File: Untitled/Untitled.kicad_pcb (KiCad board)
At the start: 2 copper layers, 8 parts

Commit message: version1
I wanna figure out how to reduce the size somehow. but this version should work fine
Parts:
- added 12v_in1: 12v_in, TestPoint:TestPoint_Pad_D2.5mm, F.Cu at (197.5, 78.1)
- added GND_in1: GND_in, TestPoint:TestPoint_Pad_D2.5mm, F.Cu at (192.4, 78.1)
- added g_out1: g_out1, TestPoint:TestPoint_Plated_Hole_D2.0mm, F.Cu at (213.9, 99.5)
- added g_out2: g_out2, TestPoint:TestPoint_Plated_Hole_D2.0mm, F.Cu at (213.9, 95.5)
- added g_out3: g_out3, TestPoint:TestPoint_Plated_Hole_D2.0mm, F.Cu at (213.9, 91.5)
- added v_out1: vout_1, TestPoint:TestPoint_Plated_Hole_D2.0mm, F.Cu at (213.8, 86.2)
- added v_out2: vout_2, TestPoint:TestPoint_Plated_Hole_D2.0mm, F.Cu at (213.8, 82.2)
- added vout_3: vout_3, TestPoint:TestPoint_Plated_Hole_D2.0mm, F.Cu at (213.8, 78.2)
- moved C2 47.9 mm to (202.3, 90.1), turned to 90 degrees
- moved R2 47.3 mm to (207.6, 81.3), turned to -90 degrees
- moved C4 44.4 mm to (204.4, 78.2), turned to 180 degrees
- moved R1 44.2 mm to (204.4, 79.8)
- moved C1 42.9 mm to (196.7, 87.2), turned to 180 degrees
- moved C3 39.8 mm to (196.7, 85.7), turned to 180 degrees
- moved L1 33.7 mm to (202.6, 84.5), turned to -90 degrees
- moved VR1 30.4 mm to (197.7, 89.7)
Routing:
- net +5V: track 0.00 -> 34.1 mm
- net Net-(VR1-VFB): track 0.00 -> 24.4 mm
- net Net-(VR1-SW): track 0.00 -> 18.8 mm, vias 0 -> 2
- net +12V: track 0.00 -> 15.3 mm
- net GND: track 0.00 -> 6.90 mm, vias 0 -> 3
- net Net-(VR1-VBST): track 0.00 -> 4.28 mm
- added copper zone on B.Cu, net GND
- added copper zone on F.Cu, net GND
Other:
- board outline added: 26 x 26.7 mm

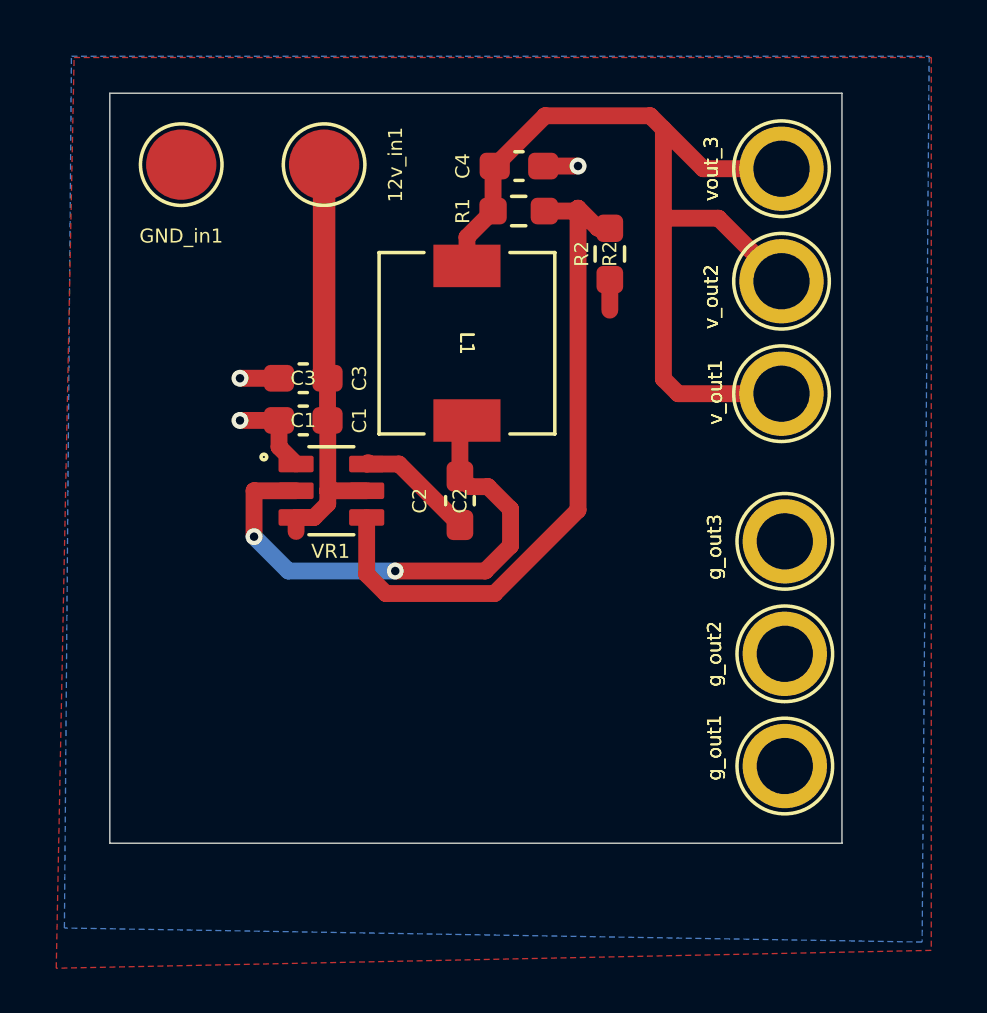
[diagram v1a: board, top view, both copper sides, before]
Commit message: updated c4 to 1206
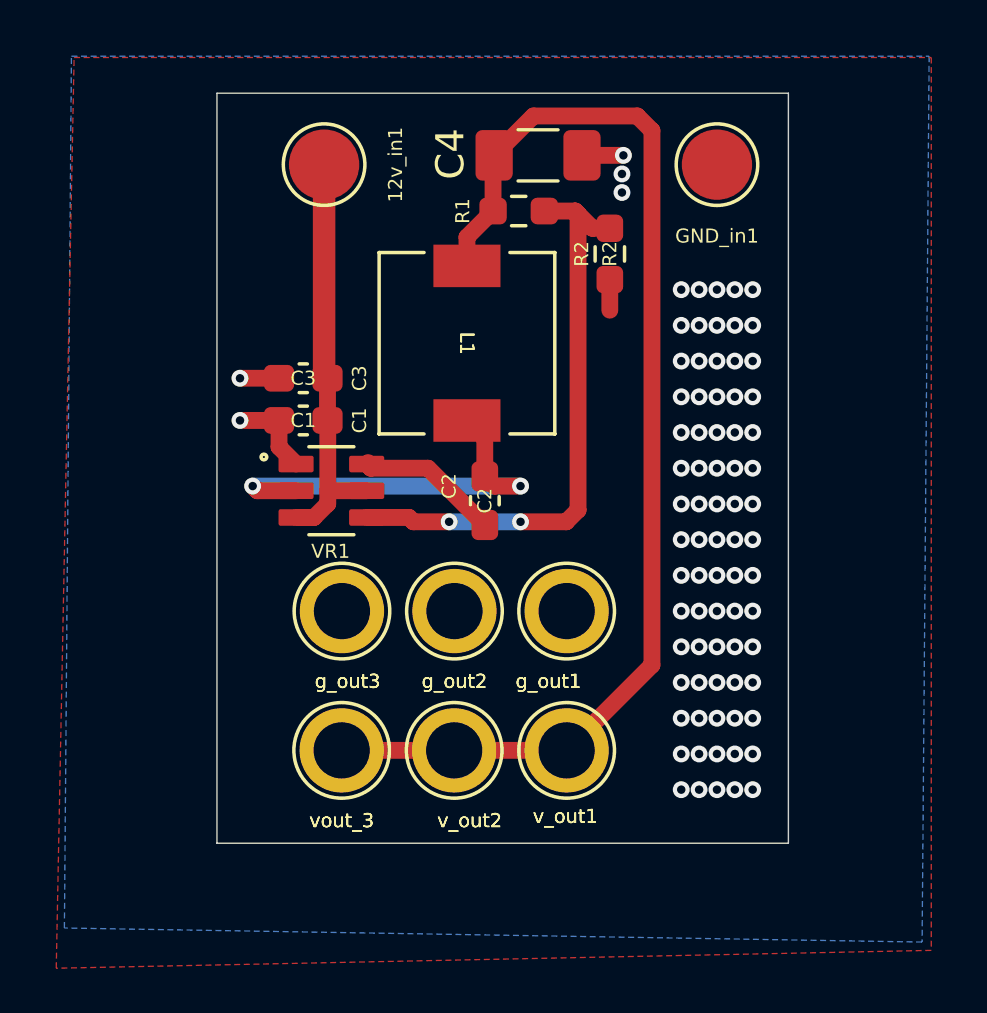
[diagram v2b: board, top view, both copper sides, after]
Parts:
- C4: footprint Capacitor_SMD:C_0603_1608Metric_Pad1.08x0.95mm_HandSolder -> Capacitor_SMD:C_1206_3216Metric_Pad1.33x1.80mm_HandSolder
- moved vout_3 25.9 mm to (198.1, 98.9), turned to 180 degrees
- moved v_out2 20.3 mm to (202.1, 98.9), turned to 180 degrees
- moved GND_in1 19.1 mm to (211.5, 78.1)
- moved g_out3 15.9 mm to (198.1, 94.0), turned to 0 degrees
- moved v_out1 14.8 mm to (206.1, 98.9), turned to 180 degrees
- moved g_out2 11.8 mm to (202.1, 94.0), turned to 180 degrees
- moved g_out1 9.52 mm to (206.1, 94.0), turned to 0 degrees
- moved C2 0.88 mm to (203.2, 90.1)
- moved C4 0.78 mm to (205.1, 77.8)
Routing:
- net +5V: track 34.1 -> 42.0 mm
- net Net-(VR1-SW): track 18.8 -> 15.2 mm
- net Net-(VR1-VFB): track 24.4 -> 21.0 mm, vias 0 -> 2
- net Net-(VR1-VBST): track 4.28 -> 5.17 mm
- net GND: track 6.90 -> 7.14 mm, vias 3 -> 80
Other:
- board size 26 x 26.7 mm -> 20.3 x 26.7 mm

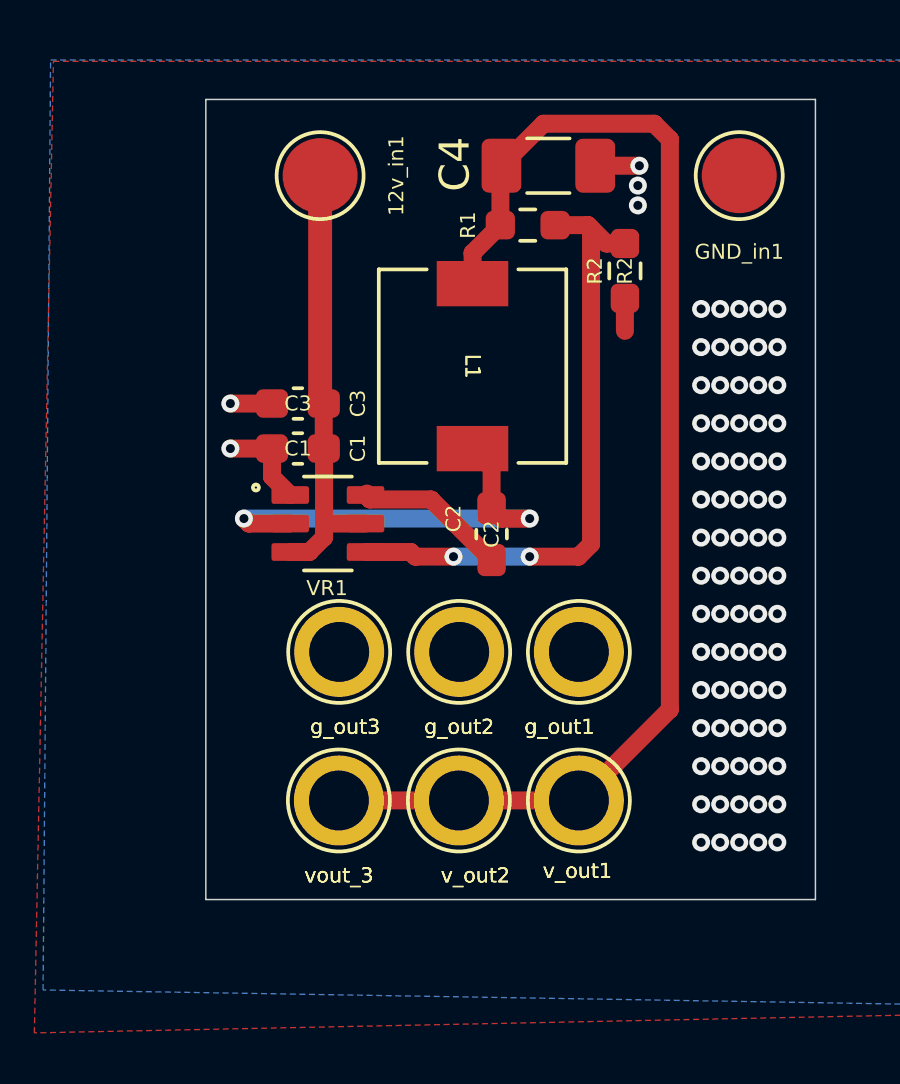
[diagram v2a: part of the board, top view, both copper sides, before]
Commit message: updated to 2.54tht pads
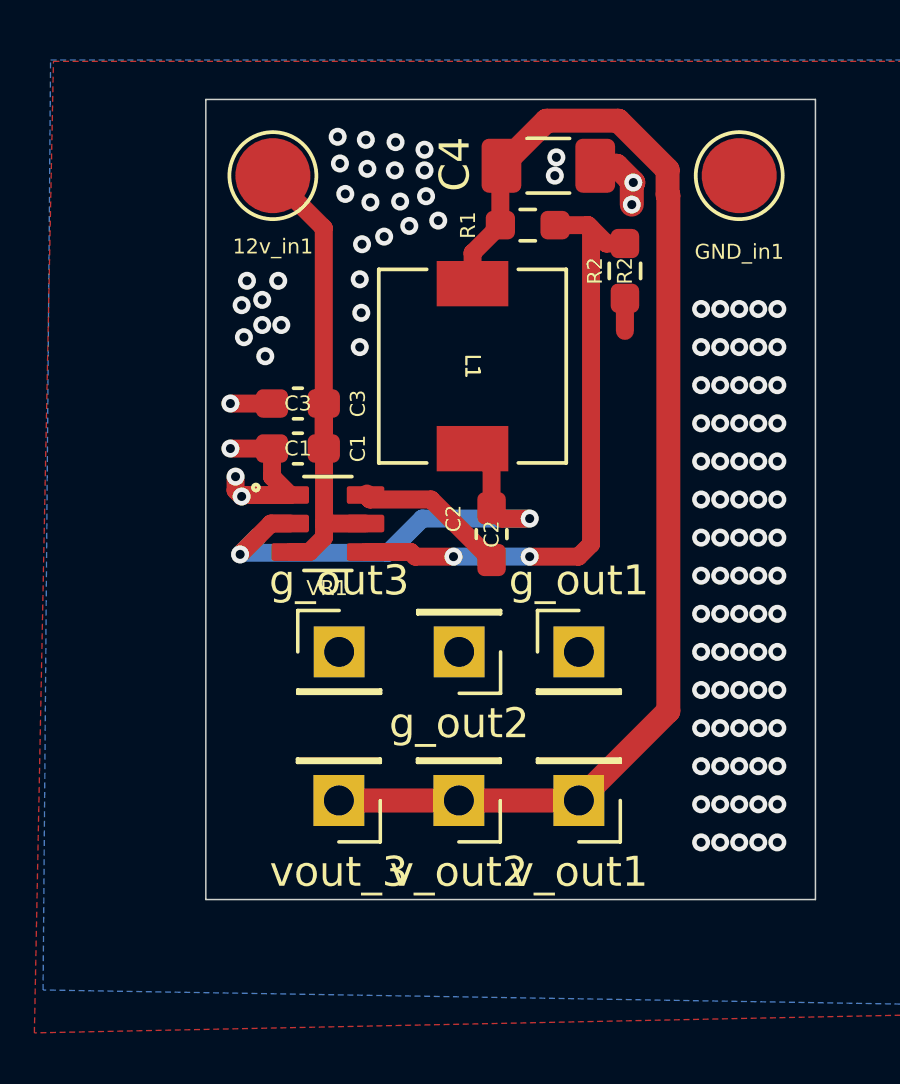
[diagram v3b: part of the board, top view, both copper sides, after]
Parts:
- g_out1, g_out2, g_out3, v_out1, v_out2, vout_3: footprint TestPoint:TestPoint_Plated_Hole_D2.0mm -> Connector_PinHeader_2.54mm:PinHeader_1x01_P2.54mm_Vertical
- moved 12v_in1 1.57 mm to (195.9, 78.1)
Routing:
- net GND: track 7.14 -> 10.3 mm, vias 80 -> 110
- net +12V: track 14.8 -> 17.6 mm
- net Net-(VR1-SW): track 15.2 -> 17.1 mm
- net +5V: track 42.0 -> 41.4 mm
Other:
- board text added: "Designed by Caleb Murray IEEE 2026"

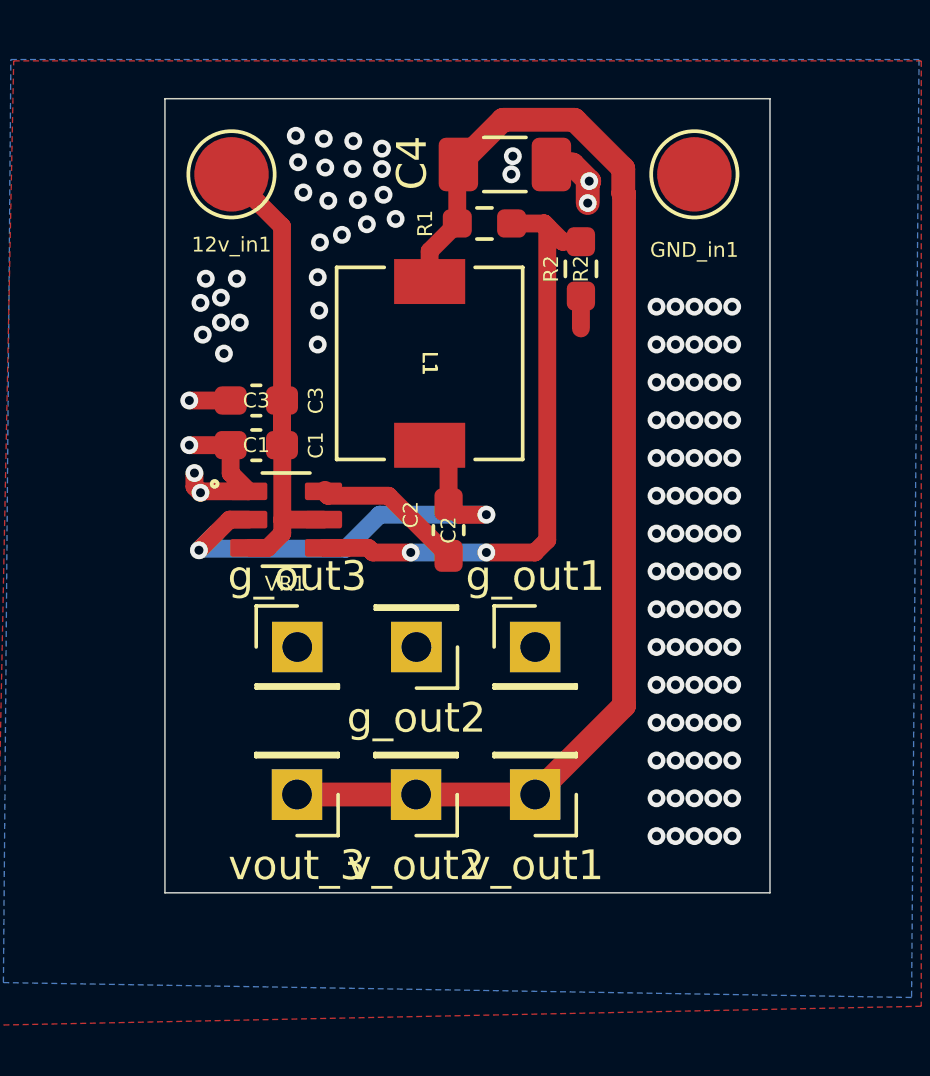
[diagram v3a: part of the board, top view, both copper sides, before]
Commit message: made prod. sent to daniel
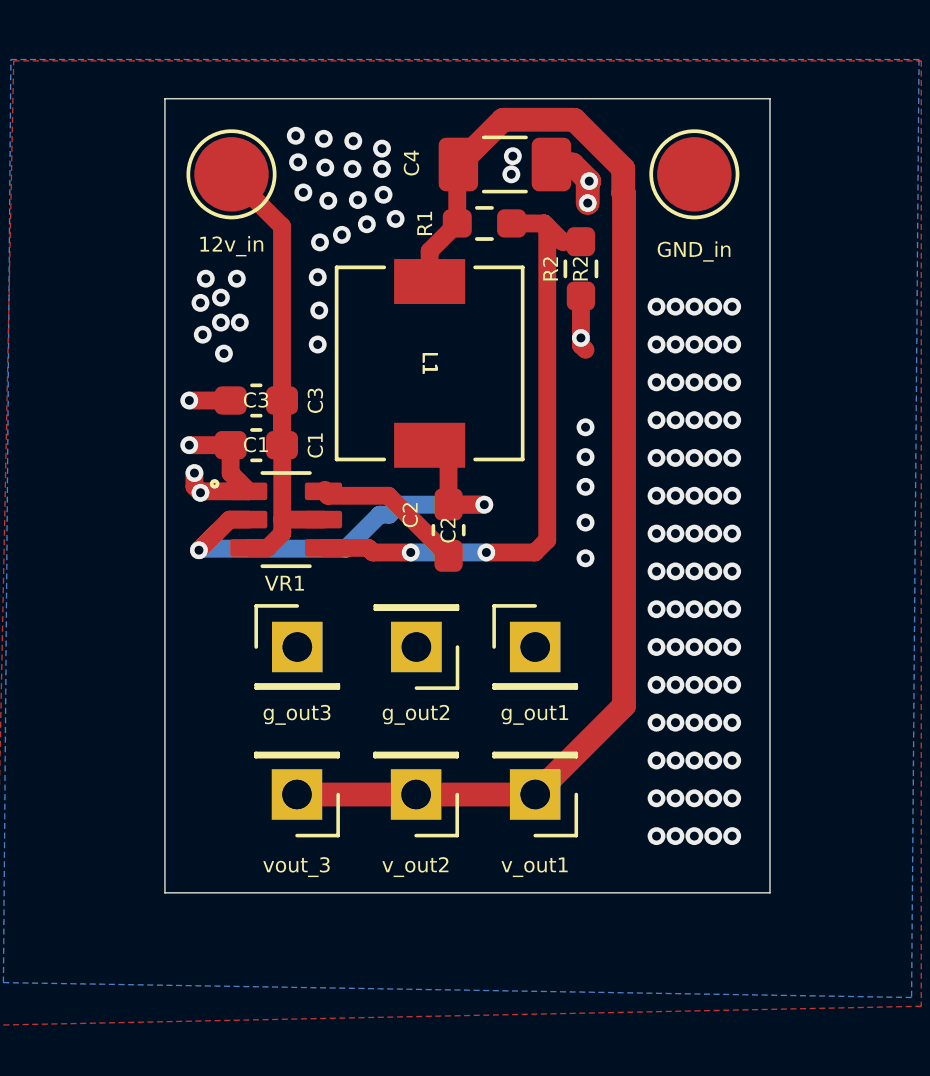
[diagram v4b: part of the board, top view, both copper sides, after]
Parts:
- renumbered 12v_in1 to 12v_in, GND_in1 to GND_in
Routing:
- net GND: track 10.3 -> 11.1 mm, vias 110 -> 116
